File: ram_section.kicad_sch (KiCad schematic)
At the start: 9 parts, among them IC1 ECP5-BGA256, U10 HyperRAM

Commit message: rename libraries from luna to cynthion
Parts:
- IC1: footprint luna:lattice_cabga256 -> cynthion:lattice_cabga256
- U10: footprint luna:BGA-24_5x5_6.0x8.0mm -> cynthion:BGA-24_5x5_6.0x8.0mm
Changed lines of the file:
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@@
     (property "Reference" "U10" (id 0) (at 137.16 99.7712 0))
     (property "Value" "HyperRAM" (id 1) (at 137.16 102.0572 0))
-    (property "Footprint" "luna:BGA-24_5x5_6.0x8.0mm" (id 2) (at 121.92 146.05 0)
+    (property "Footprint" "cynthion:BGA-24_5x5_6.0x8.0mm" (id 2) (at 121.92 146.05 0)
       (effects (font (size 1.27 1.27)) hide)
     )
@@
       (effects (font (size 1.27 1.27)) (justify right))
     )
-    (property "Footprint" "luna:lattice_cabga256" (id 2) (at -38.1 -46.99 0)
+    (property "Footprint" "cynthion:lattice_cabga256" (id 2) (at -38.1 -46.99 0)
       (effects (font (size 1.27 1.27)) (justify left) hide)
     )

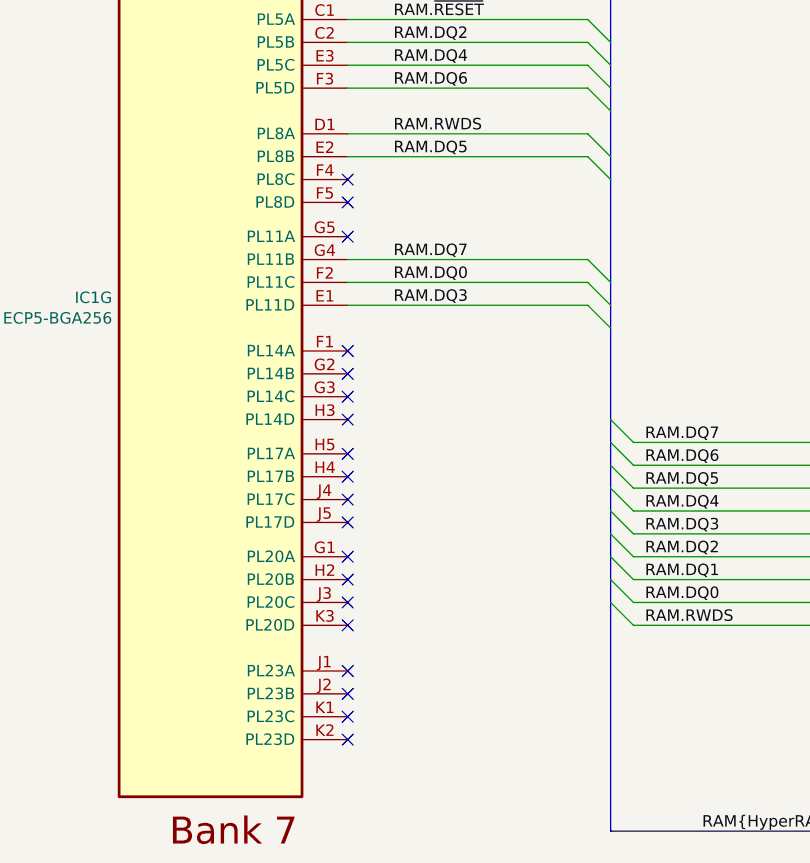
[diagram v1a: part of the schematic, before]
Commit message: Add pseudo-VCCIO and pseudo-GND pins, decoupling
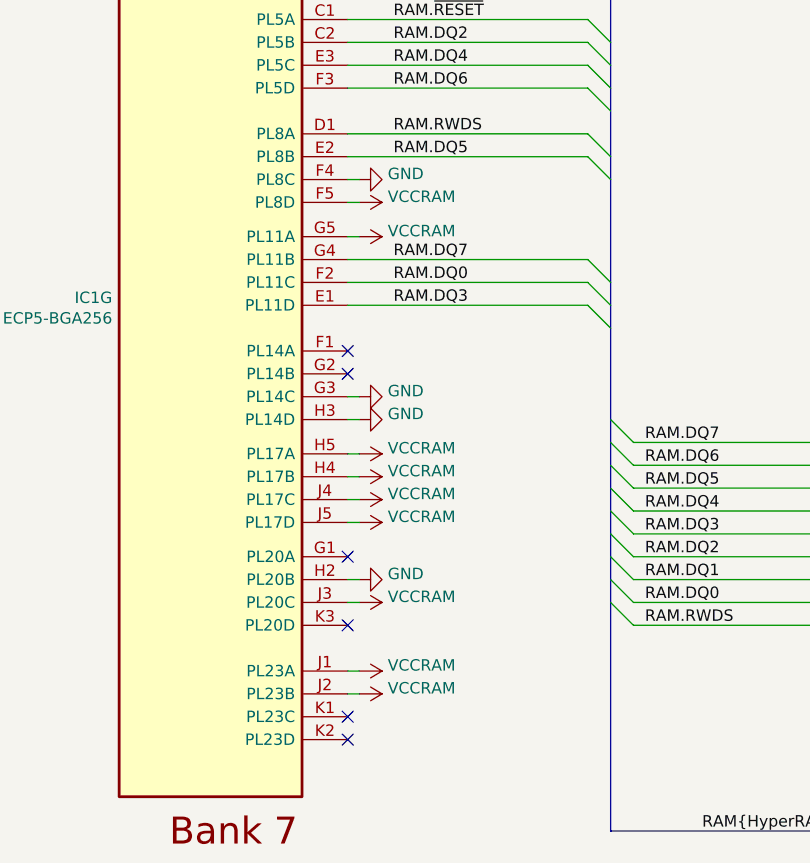
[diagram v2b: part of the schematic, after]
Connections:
- net GND: now also IC1.F4 (PL8C), IC1.G3 (PL14C), IC1.H2 (PL20B), IC1.H3 (PL14D)
- net VCCRAM: now also IC1.F5 (PL8D), IC1.G5 (PL11A), IC1.H4 (PL17B), IC1.H5 (PL17A), IC1.J1 (PL23A), IC1.J2 (PL23B), IC1.J3 (PL20C), IC1.J4 (PL17C), IC1.J5 (PL17D)
- no-connect marks 24 -> 11

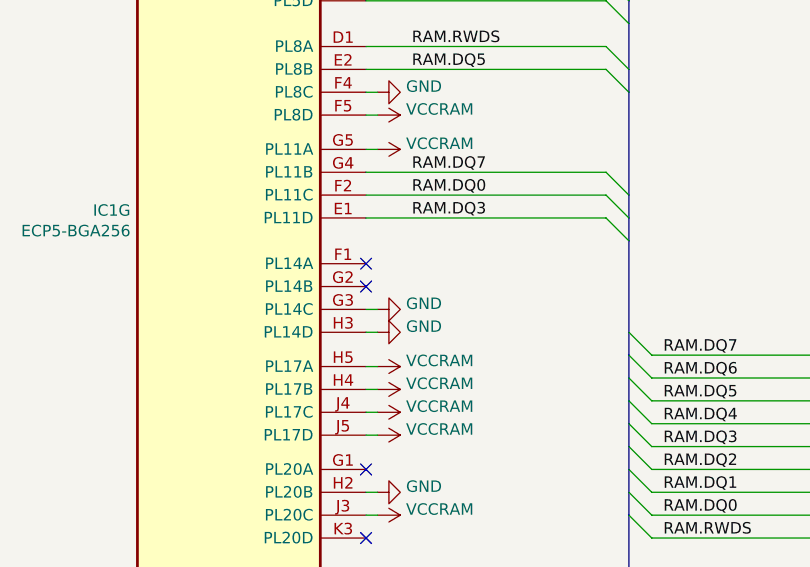
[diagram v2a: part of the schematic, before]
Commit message: Add more FPGA supply vias
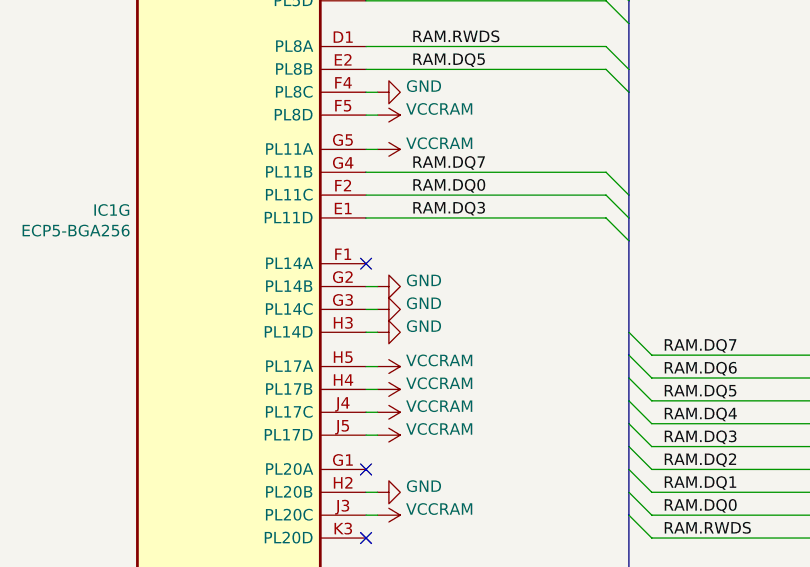
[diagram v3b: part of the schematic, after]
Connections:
- net GND: now also IC1.G2 (PL14B)
- no-connect marks 11 -> 10
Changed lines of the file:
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@@
   (no_connect (at 152.4 130.81))
   (no_connect (at 68.58 130.81))
-  (no_connect (at 68.58 102.87))
   (no_connect (at 121.92 140.97))
   (no_connect (at 68.58 100.33))
@@
   )
   (wire (pts (xy 234.95 119.38) (xy 227.33 119.38))
+    (stroke (width 0) (type default) (color 0 0 0 0))
+  )
+  (wire (pts (xy 68.58 102.87) (xy 69.85 102.87))
     (stroke (width 0) (type default) (color 0 0 0 0))
   )
@@
       (effects (font (size 1.27 1.27)) hide)
     )
+    (pin "1")
+  )
+  (symbol (lib_id "power:GND") (at 69.85 102.87 90) (unit 1)
+    (in_bom yes) (on_board yes)
+    (property "Reference" "#PWR0229" (id 0) (at 76.2 102.87 0)
+      (effects (font (size 1.27 1.27)) hide)
+    )
+    (property "Value" "GND" (id 1) (at 73.025 102.235 90)
+      (effects (font (size 1.27 1.27)) (justify right))
+    )
+    (property "Footprint" "" (id 2) (at 69.85 102.87 0)
+      (effects (font (size 1.27 1.27)) hide)
+    )
+    (property "Datasheet" "" (id 3) (at 69.85 102.87 0)
+      (effects (font (size 1.27 1.27)) hide)
+    )
